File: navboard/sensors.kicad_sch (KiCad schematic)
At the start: 4 parts, among them U1 BMM350

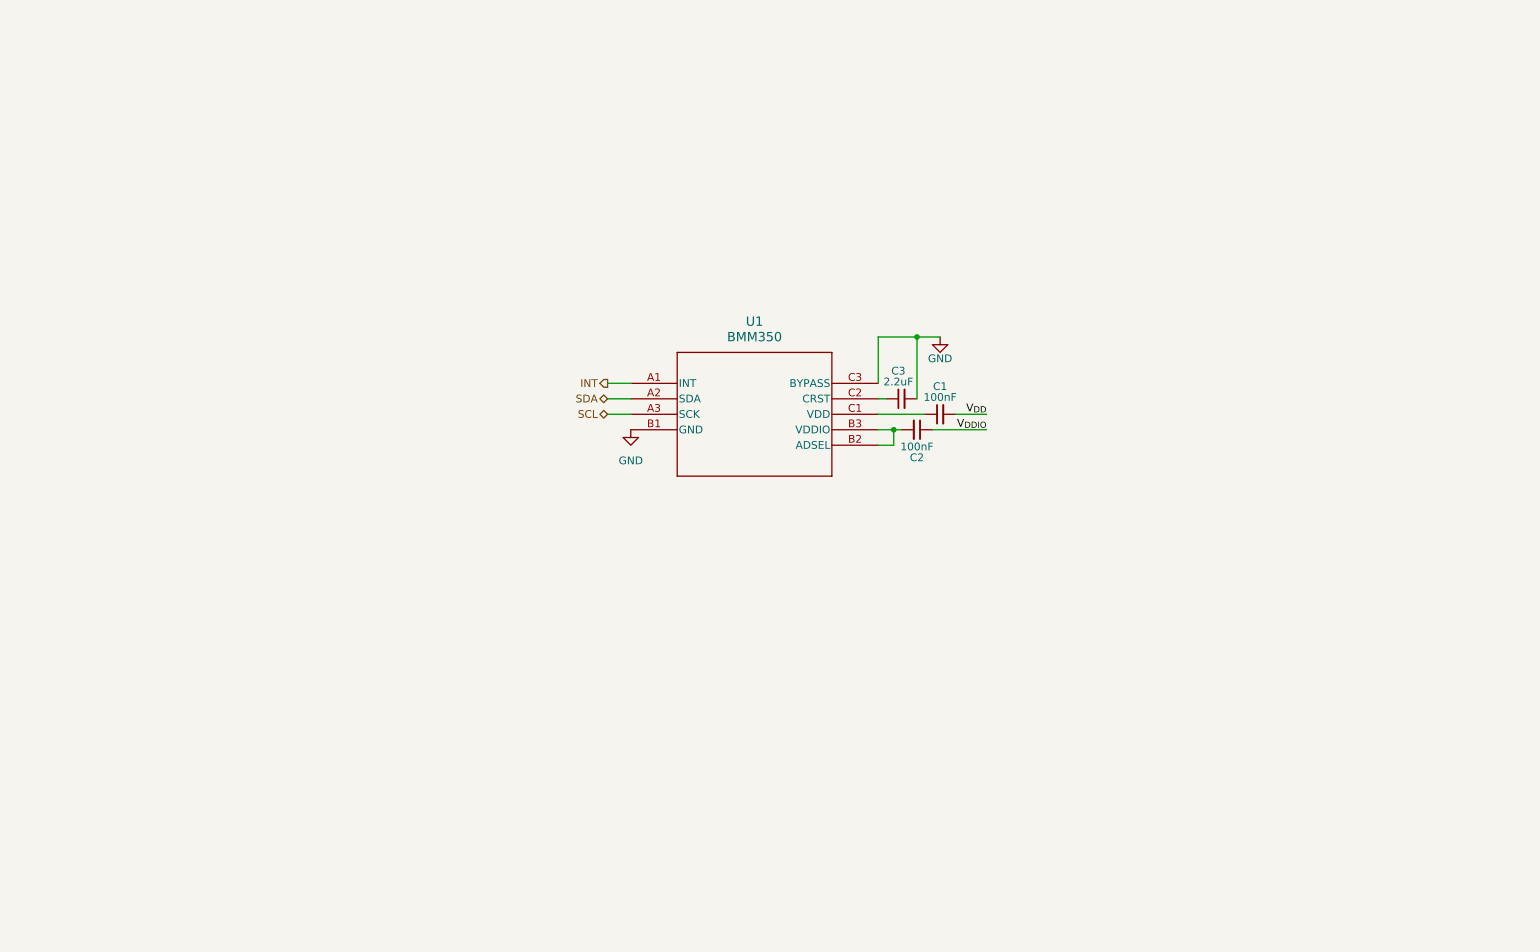
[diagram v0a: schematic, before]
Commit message: Feat[navboard]: Sensor Schematic
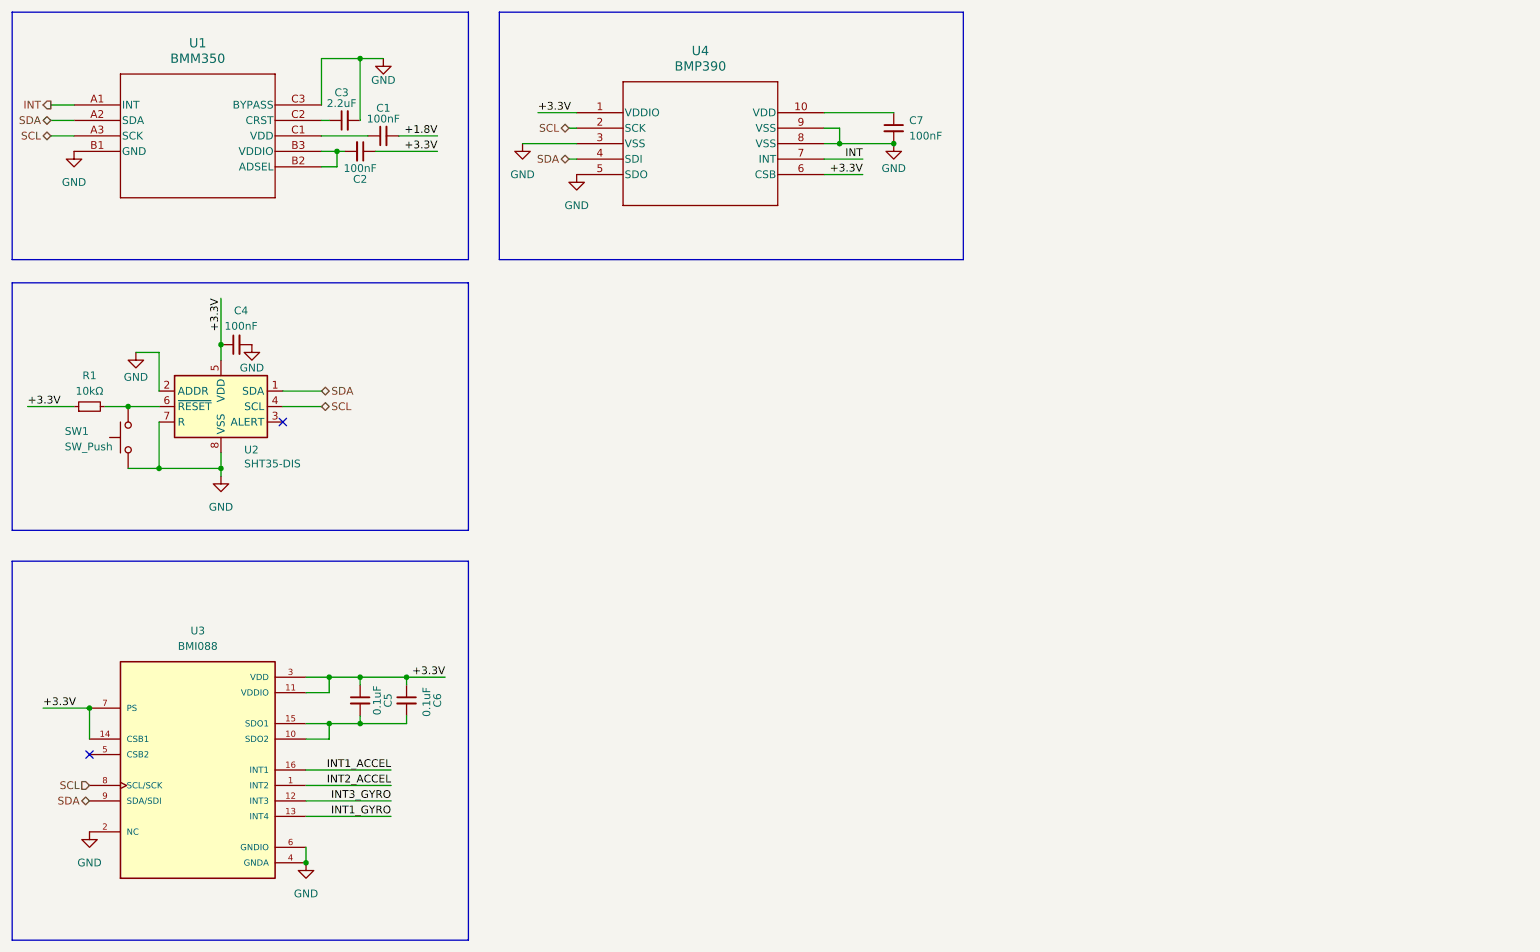
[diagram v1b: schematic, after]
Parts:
- added C4, C7: 100nF, symbol Device:C_Small
- added C5, C6: 0.1uF, symbol Device:C_Small
- added R1: 10kΩ, symbol Device:R_Small
- added SW1: SW_Push, symbol Switch:SW_Push
- added U2: SHT35-DIS, Sensor_Humidity:Sensirion_DFN-8-1EP_2.5x2.5mm_P0.5mm_EP1.1x1.7mm, symbol Sensor_Humidity:SHT35-DIS
- added U3: BMI088, PQFN50P450X300X100-16N, symbol BMI088:BMI088
- added U4: BMP390, 10LGA_2X2X0p75_BOS, symbol BMP390:BMP390
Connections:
- net GND: now also C4.2, C7.2, SW1.1, U2.2 (ADDR), U2.7 (R), U2.8 (VSS), U2.9 (VSS), U3.2 (NC), U3.4 (GNDA), U3.6 (GNDIO), U4.3 (VSS), U4.5 (SDO), U4.8 (VSS), U4.9 (VSS)
- net INT: now also U4.7 (INT)
- net SCL: now also U2.4 (SCL), U3.8 (SCL/SCK), U4.2 (SCK)
- net SDA: now also U2.1 (SDA), U3.9 (SDA/SDI), U4.4 (SDI)
- net V_{DDIO} renamed +3.3V
- net +3.3V: now also C4.1, C5.1, C6.1, R1.1, U2.5 (VDD), U3.11 (VDDIO), U3.14 (CSB1), U3.3 (VDD), U3.7 (PS), U4.1 (VDDIO), U4.6 (CSB)
- net V_{DD} renamed +1.8V
- new net: C5.2, C6.2, U3.10 (SDO2), U3.15 (SDO1)
- new net: C7.1, U4.10 (VDD)
- new net: R1.2, SW1.2, U2.6 (~{RESET})
- new net INT1_ACCEL: U3.16 (INT1)
- new net INT1_GYRO: U3.13 (INT4)
- new net INT2_ACCEL: U3.1 (INT2)
- new net INT3_GYRO: U3.12 (INT3)
- no-connect marks 0 -> 2
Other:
- moved on the sheet: C1, C2, C3, U1

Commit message: Feat[navboard]: Additional Sensors Schematic
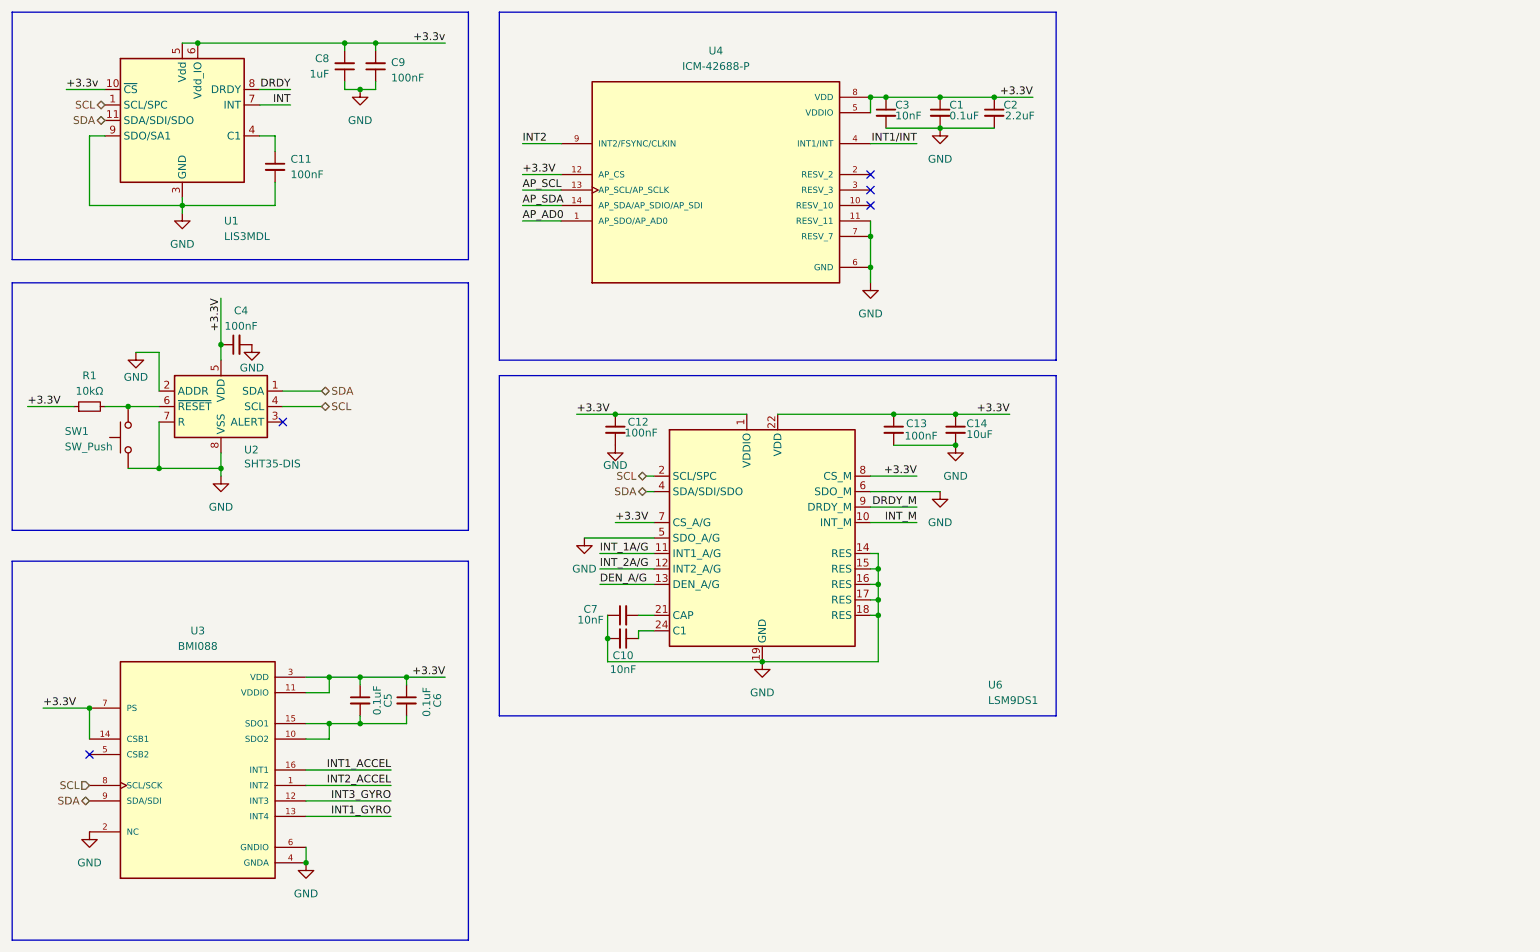
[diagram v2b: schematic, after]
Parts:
- removed U1: BMM350, BGA9_BMM350_BOS, symbol BMM350:BMM350
- removed U4: BMP390, 10LGA_2X2X0p75_BOS, symbol BMP390:BMP390
- added C10: 10nF, symbol Device:C_Small
- added C11, C9: 100nF, Capacitor_SMD:C_0402_1005Metric, symbol Device:C_Small
- added C12, C13: 100nF, symbol Device:C_Small
- added C14: 10uF, symbol Device:C_Small
- added C8: 1uF, Capacitor_SMD:C_0402_1005Metric, symbol Device:C_Small
- added U1: LIS3MDL, Package_LGA:LGA-12_2x2mm_P0.5mm, symbol Sensor_Magnetic:LIS3MDL
- added U4: ICM-42688-P, ICM-42688-P:PQFN50P300X250X97-14N, symbol ICM-42688-P:ICM-42688-P
- added U6: LSM9DS1, Package_LGA:LGA-24L_3x3.5mm_P0.43mm, symbol Sensor_Motion:LSM9DS1
- C1: value 100nF -> 0.1uF
- C2: value 100nF -> 2.2uF
- C3: value 2.2uF -> 10nF
- C7: value 100nF -> 10nF
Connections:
- net +1.8V is gone; now on net GND: C1.2
- net +3.3V: now also C1.1, C3.1, C12.1, C13.1, C14.1, U4.12 (AP_CS), U4.5 (VDDIO), U4.8 (VDD), U6.1 (VDDIO), U6.22 (VDD), U6.23 (VDD), U6.3 (VDDIO), U6.7 (CS_A/G), U6.8 (CS_M)
- net GND: now also C2.2, C7.1, C10.2, C11.2, C12.2, C13.2, C14.2, C8.1, C9.1, U1.12 (GND), U1.2 (GND), U1.3 (GND), U1.9 (SDO/SA1), U4.11 (RESV_11), U4.6 (GND), U4.7 (RESV_7), U6.14 (RES), U6.15 (RES), U6.16 (RES), U6.17 (RES), U6.18 (RES), U6.19 (GND), U6.20 (GND), U6.5 (SDO_A/G), U6.6 (SDO_M); no longer C7.2
- net INT: now also U1.7 (INT)
- net SCL: now also U1.1 (SCL/SPC), U6.2 (SCL/SPC)
- net SDA: now also U1.11 (SDA/SDI/SDO), U6.4 (SDA/SDI/SDO)
- new net: C10.1, U6.24 (C1)
- new net: C7.2, U6.21 (CAP)
- new net: C11.1, U1.4 (C1)
- new net +3.3v: C8.2, C9.2, U1.10 (~{CS}), U1.5 (Vdd), U1.6 (Vdd_IO)
- new net AP_AD0: U4.1 (AP_SDO/AP_AD0)
- new net AP_SCL: U4.13 (AP_SCL/AP_SCLK)
- new net AP_SDA: U4.14 (AP_SDA/AP_SDIO/AP_SDI)
- new net DEN_A/G: U6.13 (DEN_A/G)
- new net DRDY: U1.8 (DRDY)
- new net DRDY_M: U6.9 (DRDY_M)
- new net INT1/INT: U4.4 (INT1/INT)
- new net INT2: U4.9 (INT2/FSYNC/CLKIN)
- new net INT_1A/G: U6.11 (INT1_A/G)
- new net INT_2A/G: U6.12 (INT2_A/G)
- new net INT_M: U6.10 (INT_M)
- no-connect marks 2 -> 5

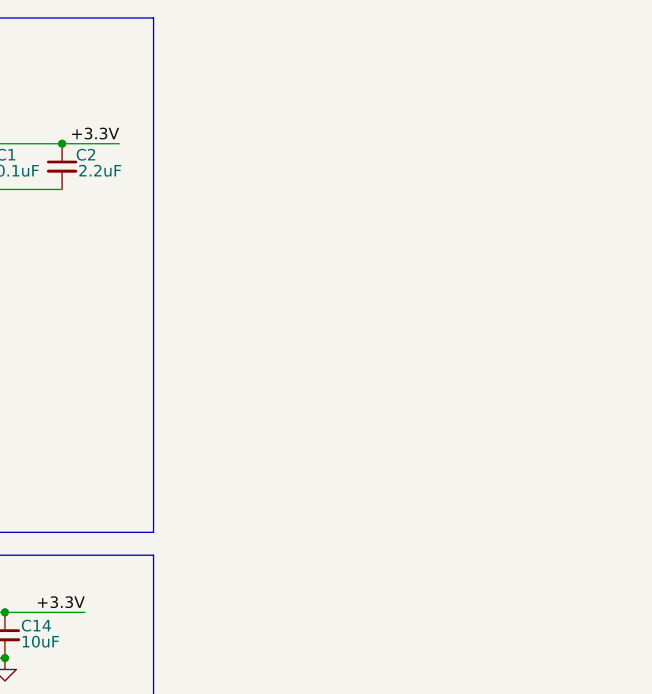
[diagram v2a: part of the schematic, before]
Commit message: Feat[navboard]: BMM150 schematic
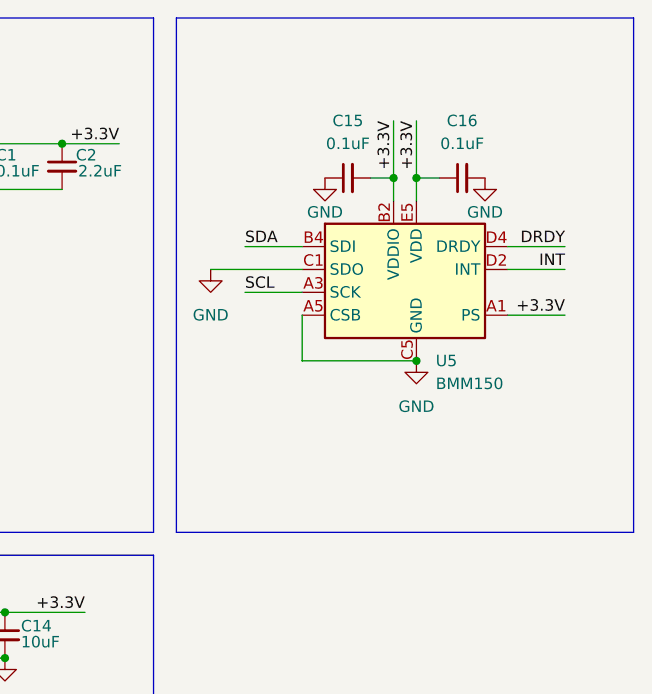
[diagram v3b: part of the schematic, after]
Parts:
- added C15, C16: 0.1uF, symbol Device:C_Small
- added U5: BMM150, Package_CSP:WLCSP-12_1.56x1.56mm_P0.4mm, symbol Sensor_Magnetic:BMM150
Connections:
- net +3.3V: now also C15.2, C16.1, U5.A1 (PS), U5.B2 (VDDIO), U5.E5 (VDD)
- net DRDY: now also U5.D4 (DRDY)
- net GND: now also C15.1, C16.2, U5.A5 (CSB), U5.C1 (SDO), U5.C5 (GND), U5.E1 (GND), U5.E3 (GND)
- net INT: now also U5.D2 (INT)
- net SCL: now also U5.A3 (SCK)
- net SDA: now also U5.B4 (SDI)
